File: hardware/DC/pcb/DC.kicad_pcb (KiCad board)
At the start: 2 copper layers, 105 x 63 mm, 51 parts, among them J1 POWER, Q1 S8050, SW1 SW_SPDT, SW2 SW_Push_Dual, SW3 SW_Push_Dual, U1 LM2672M-5.0, U2 ESP-32_NodeMCU, U3 74HC595, U4 HD44780, U5 MCP3208

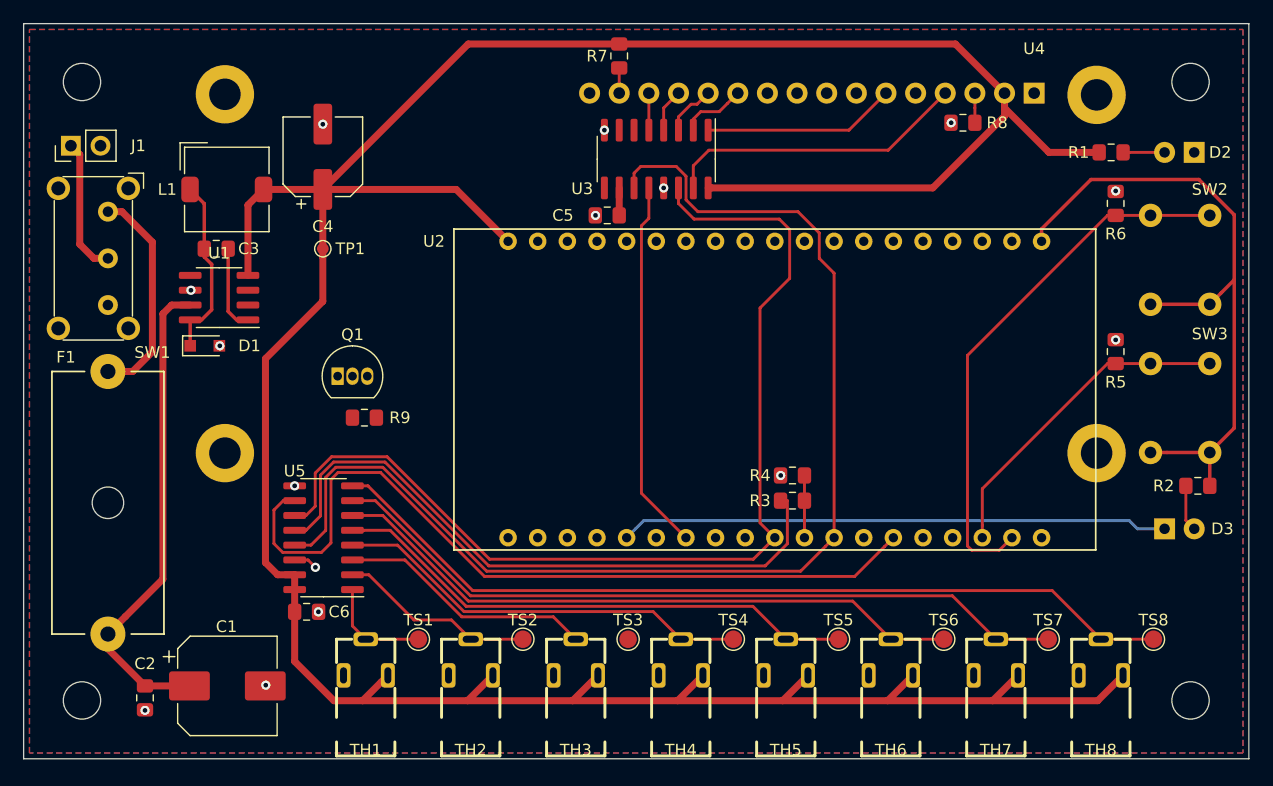
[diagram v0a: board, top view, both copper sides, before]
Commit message: feat: Split 5V rail from main PCB
split 5 V from PCB, remove old stuff

Issue #51
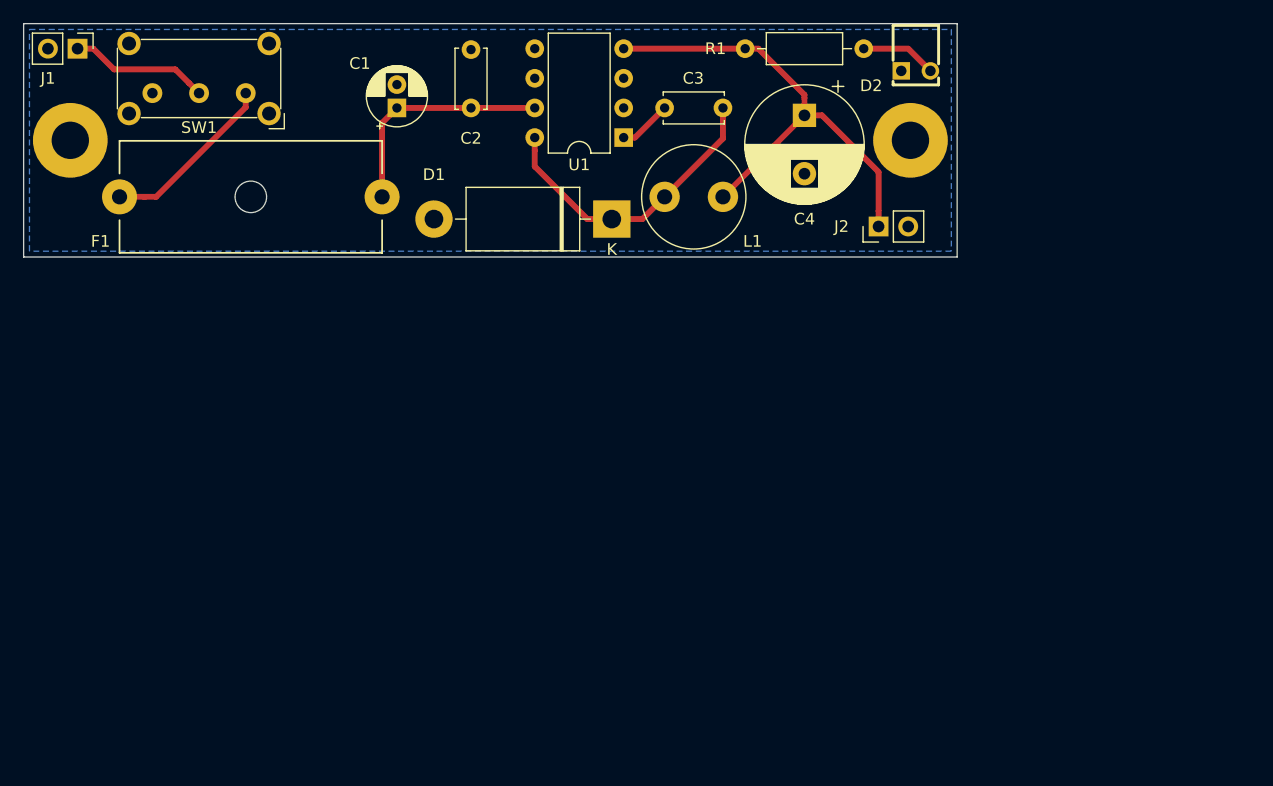
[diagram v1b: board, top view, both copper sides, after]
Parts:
- removed C5, C6: 100n, Resistor_SMD:R_0805_2012Metric_Pad1.15x1.40mm_HandSolder
- removed D3: GREEN, LED_THT:LED_D3.0mm
- removed Q1: S8050, Package_TO_SOT_THT:TO-92_Inline
- removed R2: 140, Resistor_SMD:R_0805_2012Metric_Pad1.15x1.40mm_HandSolder
- removed R3: 1k, Resistor_SMD:R_0805_2012Metric_Pad1.15x1.40mm_HandSolder
- removed R4, R5, R6, R9: 2k2, Resistor_SMD:R_0805_2012Metric_Pad1.15x1.40mm_HandSolder
- removed R7: 220, Resistor_SMD:R_0805_2012Metric_Pad1.15x1.40mm_HandSolder
- removed R8: 2k, Resistor_SMD:R_0805_2012Metric_Pad1.15x1.40mm_HandSolder
- removed SW2, SW3: SW_Push_Dual, NAMAE:NAMAE_JTP-1130P
- removed TH1, TH2, TH3, TH4, TH5, TH6, TH7, TH8: AudioJack3, Lumberg:LUMBERG_1501_05
- removed TP1: TestPoint, TestPoint:TestPoint_Pad_D1.0mm
- removed TS1, TS2, TS3, TS4, TS5, TS6, TS7, TS8: TestPoint, TestPoint:TestPoint_Pad_D1.5mm
- removed U2: ESP-32_NodeMCU, Collection:ESP-32_NodeMCU
- removed U3: 74HC595, Package_SO:SOIC-16_3.9x9.9mm_P1.27mm
- removed U4: HD44780, Collection:HD44780_LCD_2x16
- removed U5: MCP3208, Package_SO:SOIC-16_3.9x9.9mm_P1.27mm
- removed the ~ at (115.0, 73.0)
- removed the ~ at (115.0, 20.0)
- removed the ~ at (20.0, 73.0)
- removed the ~ at (20.0, 20.0)
- added J2: OUTPUT, Connector_PinHeader_2.54mm:PinHeader_1x02_P2.54mm_Vertical, F.Cu at (88.3, 32.4)
- added ~: MountingHole_3.2mm_M3_Pad, MountingHole:MountingHole_3.2mm_M3_Pad, F.Cu at (91.0, 25.0)
- added ~: MountingHole_3.2mm_M3_Pad, MountingHole:MountingHole_3.2mm_M3_Pad, F.Cu at (19.0, 25.0)
- C1: footprint Capacitor_SMD:CP_Elec_8x10 -> Capacitor_THT:CP_Radial_D5.0mm_P2.00mm
- C2, C3: footprint Resistor_SMD:R_0805_2012Metric_Pad1.15x1.40mm_HandSolder -> Capacitor_THT:C_Disc_D5.0mm_W2.5mm_P5.00mm
- C4: footprint Capacitor_SMD:CP_Elec_6.3x5.9 -> Capacitor_THT:CP_Radial_D10.0mm_P5.00mm
- D1: footprint Diode_SMD:D_SOD-323_HandSoldering -> Diode_THT:D_DO-201AD_P15.24mm_Horizontal
- D2: footprint LED_THT:LED_D3.0mm -> VCC:5600F; moved to F.Cu
- L1: footprint Inductor_SMD:L_TDK_SLF7032 -> Inductor_THT:L_Radial_D8.7mm_P5.00mm_Fastron_07HCP
- R1: footprint Resistor_SMD:R_0805_2012Metric_Pad1.15x1.40mm_HandSolder -> Resistor_THT:R_Axial_DIN0207_L6.3mm_D2.5mm_P10.16mm_Horizontal
- U1: footprint Package_SO:SOIC-8_3.9x4.9mm_P1.27mm -> Package_DIP:DIP-8_W7.62mm
- moved C2 57.8 mm to (53.3, 22.2), turned to 90 degrees
- moved C1 51.6 mm to (47.0, 22.2), turned to 90 degrees
- moved C3 45.1 mm to (74.9, 22.2), turned to 180 degrees
- moved F1 44.2 mm to (45.7, 29.8), turned to 180 degrees
- moved C4 41.4 mm to (81.9, 22.9), turned to 270 degrees
- moved L1 37.5 mm to (69.9, 29.8)
- moved U1 37.3 mm to (66.4, 24.8)
- moved D1 36.5 mm to (65.4, 31.8), turned to 180 degrees
- moved R1 32.6 mm to (76.8, 17.1), turned to 0 degrees
- moved D2 26.3 mm to (91.5, 15.1), turned to 0 degrees
- moved SW1 15.6 mm to (34.0, 21.0), turned to 180 degrees
- moved J1 8.34 mm to (19.6, 17.1), turned to 270 degrees
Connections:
- R1 pad 1: Net-(D2-Pad2) -> +5V
- R1 pad 2: +5V -> Net-(D2-Pad2)
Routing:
- net +5V: track 276.1 -> 41.8 mm
- net /SCLK: track 104.1 -> 0.00 mm
- net /MOSI: track 89.1 -> 0.00 mm
- net /SIGNAL8: track 74.1 -> 0.00 mm
- net /CS1: track 69.5 -> 0.00 mm
- net /SIGNAL7: track 64.5 -> 0.00 mm
- net +3V3: track 57.8 -> 0.00 mm
- net /MISO: track 55.4 -> 0.00 mm
- net /SIGNAL6: track 55.1 -> 0.00 mm
- net Net-(D3-Pad1): track 47.0 -> 0.00 mm
- net Net-(R6-Pad1): track 46.5 -> 0.00 mm
- net /SIGNAL5: track 45.5 -> 0.00 mm
- net /SIGNAL4: track 36.0 -> 0.00 mm
- net /CS2: track 31.8 -> 0.00 mm
- net Net-(R5-Pad1): track 28.1 -> 0.00 mm
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- removed copper zone on F.Cu, net +5V
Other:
- board size 105 x 63 mm -> 80 x 20 mm
- net class 3V3 removed
- net class 5V removed
- net class Default: trace_width 0.25 -> 0.5

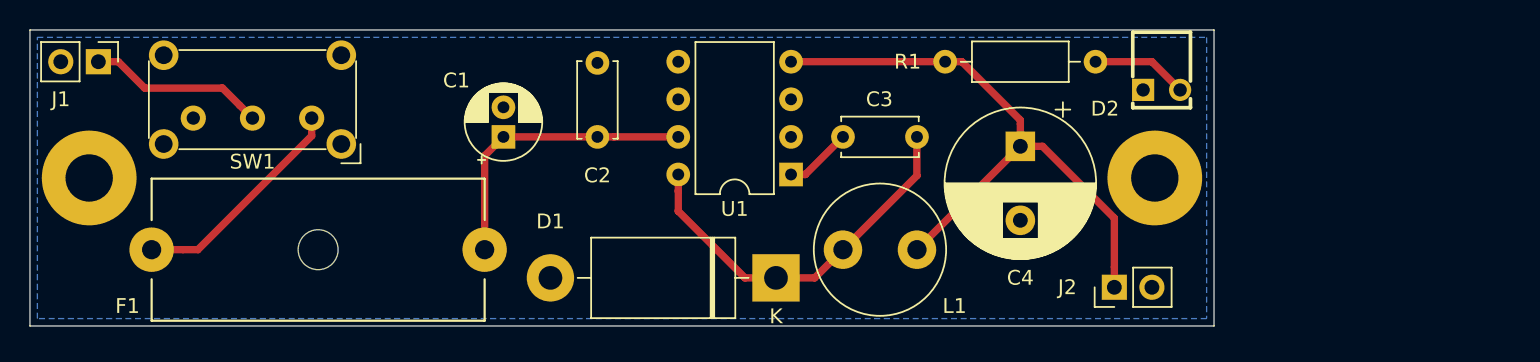
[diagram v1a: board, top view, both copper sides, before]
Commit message: feat: Use transistor to control display
redo

Issue #47
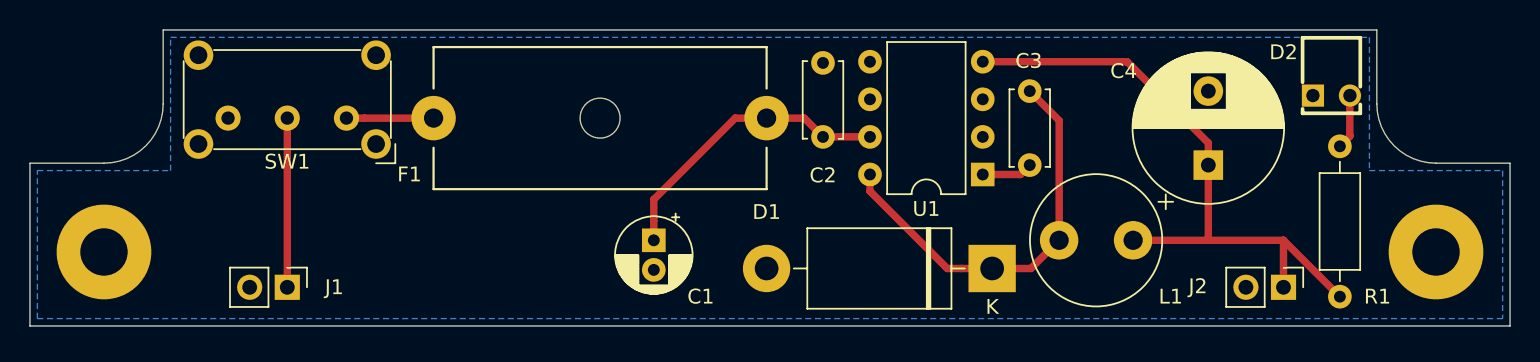
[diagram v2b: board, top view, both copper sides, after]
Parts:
- moved R1 31.0 mm to (103.5, 33.0), turned to 90 degrees
- moved F1 21.0 mm to (64.8, 21.0)
- moved J1 19.9 mm to (32.4, 32.4)
- moved ~ 19.6 mm to (110.0, 30.0)
- moved C2 15.2 mm to (68.6, 22.2)
- moved D1 14.6 mm to (80.0, 31.1)
- moved L1 14.6 mm to (84.5, 29.2)
- moved U1 13.0 mm to (79.4, 24.8)
- moved C4 12.8 mm to (94.6, 24.1), turned to 90 degrees
- moved C1 12.3 mm to (57.1, 29.2), turned to 270 degrees
- moved D2 11.5 mm to (102.9, 15.4)
- moved J2 11.4 mm to (99.7, 32.4), turned to 270 degrees
- moved C3 8.22 mm to (82.5, 19.1), turned to 270 degrees
- moved ~ 5.10 mm to (20.0, 30.0)
- moved SW1 2.35 mm to (36.4, 21.0)
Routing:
- net Net-(F1-Pad2): track 15.2 -> 5.89 mm
- net Net-(D2-Pad2): track 6.50 -> 3.71 mm
- net Net-(C3-Pad1): track 26.0 -> 27.8 mm
- net Net-(C3-Pad2): track 4.56 -> 3.44 mm
- net +5V: track 41.8 -> 42.8 mm
- net /VPOWER: track 12.0 -> 11.4 mm
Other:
- board size 80 x 20 mm -> 100 x 20 mm

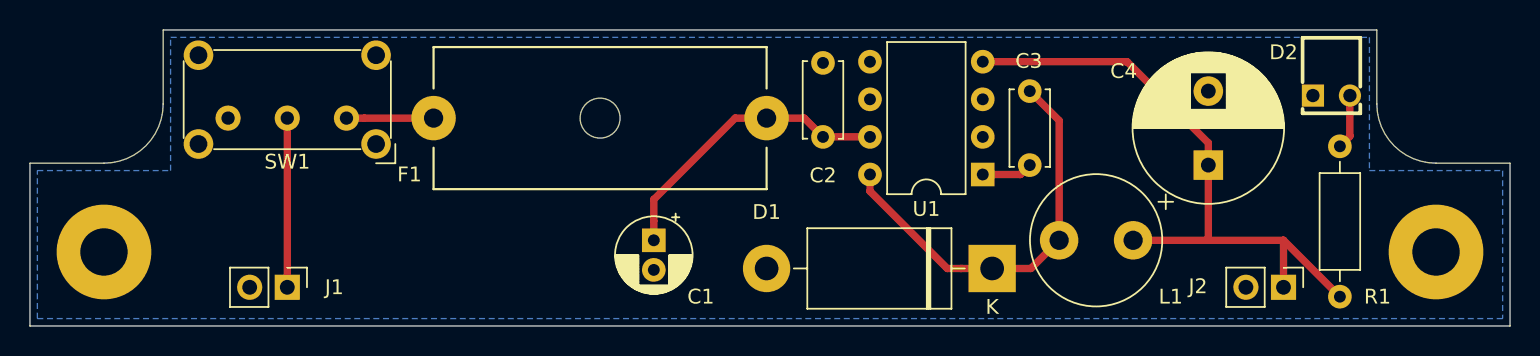
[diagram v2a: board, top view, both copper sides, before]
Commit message: feat: Split 5V rail from main PCB
redo PCB, start lid

Issue #51
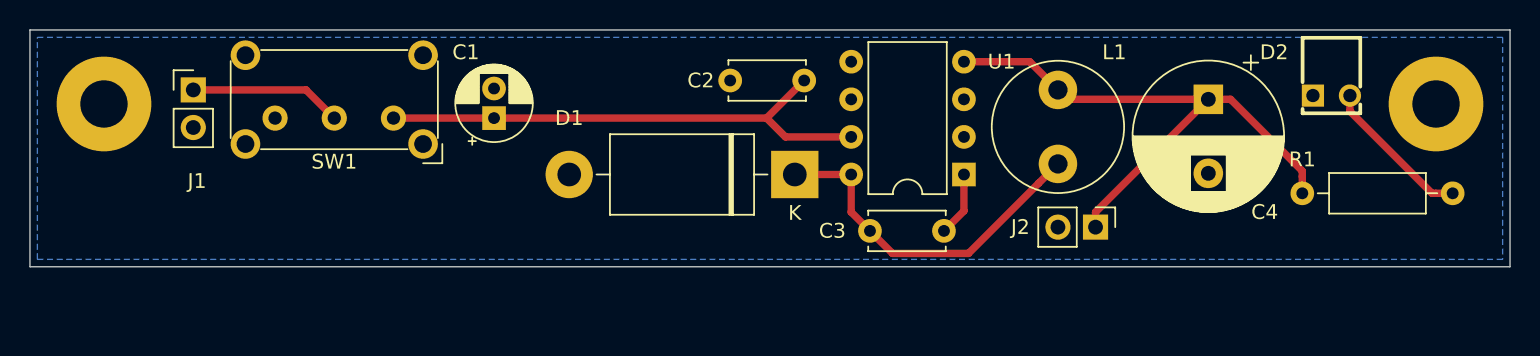
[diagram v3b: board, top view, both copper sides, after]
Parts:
- removed F1: Fuse, Schurter:Fuse_holder_20x5_22.5
- moved D1 14.8 mm to (66.7, 24.8)
- moved J1 14.8 mm to (26.0, 19.1), turned to 0 degrees
- moved C3 14.3 mm to (71.8, 28.6), turned to 0 degrees
- moved C1 13.6 mm to (46.4, 21.0), turned to 90 degrees
- moved J2 13.3 mm to (87.0, 28.3)
- moved ~ 10.0 mm to (110.0, 20.0)
- moved ~ 10.0 mm to (20.0, 20.0)
- moved R1 7.43 mm to (101.0, 26.0), turned to 0 degrees
- moved L1 5.16 mm to (84.5, 24.1), turned to 90 degrees
- moved C4 4.45 mm to (94.6, 19.7), turned to 270 degrees
- moved C2 4.02 mm to (67.3, 18.4), turned to 180 degrees
- moved SW1 3.18 mm to (39.6, 21.0)
- moved U1 1.27 mm to (78.1, 24.8)
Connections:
- SW1 pad 1: Net-(F1-Pad2) -> /VIN
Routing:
- net /VIN: track 20.2 -> 35.0 mm
- net Net-(D2-Pad2): track 3.71 -> 10.3 mm
- net Net-(F1-Pad2): track 5.89 -> 0.00 mm
- net Net-(C3-Pad1): track 27.8 -> 24.0 mm
- net +5V: track 42.8 -> 39.2 mm
- net /VPOWER: track 11.4 -> 10.3 mm
- net Net-(C3-Pad2): track 3.44 -> 4.37 mm
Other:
- board size 100 x 20 mm -> 100 x 16 mm

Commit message: feat: Use transistor to control display
resize and redo PCB

Issue #47
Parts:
- J1: footprint Connector_PinHeader_2.54mm:PinHeader_1x02_P2.54mm_Vertical -> Connector_Wire:SolderWirePad_1x02_P5.08mm_Drill1.5mm
- J2: footprint Connector_PinHeader_2.54mm:PinHeader_1x02_P2.54mm_Vertical -> Connector_PinSocket_2.54mm:PinSocket_1x02_P2.54mm_Vertical; moved to B.Cu
- moved J2 23.1 mm to (110.0, 26.0), turned to 180 degrees
- moved R1 15.0 mm to (88.9, 17.1)
- moved J1 7.85 mm to (24.1, 26.7), turned to 180 degrees
- moved L1 3.18 mm to (84.5, 27.2)
- moved C4 2.54 mm to (94.6, 22.2)
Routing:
- net +5V: track 39.2 -> 44.0 mm
- net Net-(D2-Pad2): track 10.3 -> 6.07 mm
- net /VPOWER: track 10.3 -> 13.8 mm
- net Net-(C3-Pad1): track 24.0 -> 22.7 mm

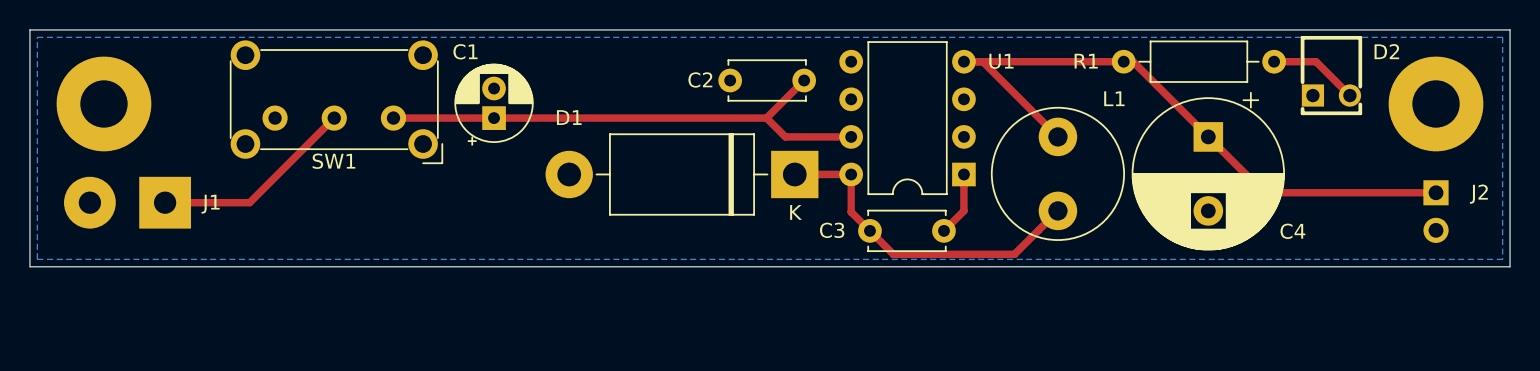
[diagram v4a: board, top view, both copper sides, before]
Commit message: feat: Firmware: Convert Temperatures
make first case

Issue #27
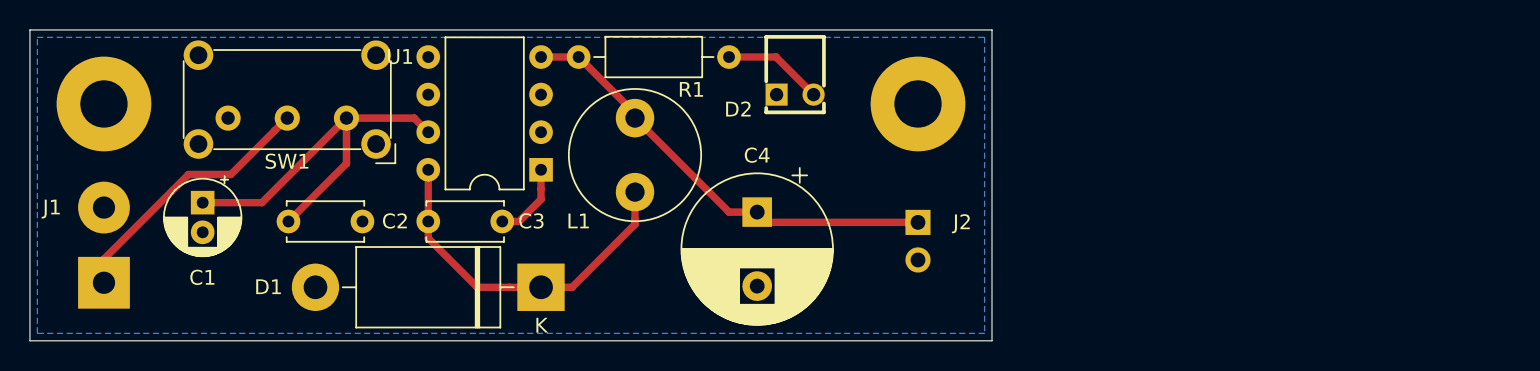
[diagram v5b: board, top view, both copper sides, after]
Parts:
- moved R1 36.8 mm to (52.1, 16.8)
- moved D2 36.2 mm to (66.7, 15.4)
- moved C2 36.1 mm to (32.5, 27.9), turned to 0 degrees
- moved J2 35.1 mm to (75.0, 28.0)
- moved ~ 35.0 mm to (75.0, 20.0)
- moved C4 30.9 mm to (64.1, 27.3)
- moved C3 29.9 mm to (41.9, 27.9)
- moved L1 28.6 mm to (55.9, 26.0)
- moved U1 28.6 mm to (49.5, 24.4)
- moved C1 20.5 mm to (26.7, 26.7), turned to 270 degrees
- moved D1 18.8 mm to (49.5, 32.4)
- moved J1 6.81 mm to (20.0, 32.1), turned to 90 degrees
- moved SW1 3.18 mm to (36.4, 21.0)
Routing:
- net +5V: track 44.0 -> 30.3 mm
- net /VIN: track 35.0 -> 26.6 mm
- net /VPOWER: track 13.8 -> 17.9 mm
- net Net-(C3-Pad1): track 22.7 -> 23.9 mm
- net Net-(C3-Pad2): track 4.37 -> 5.24 mm
- net Net-(D2-Pad2): track 6.07 -> 6.77 mm
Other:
- board size 100 x 16 mm -> 65 x 21 mm
